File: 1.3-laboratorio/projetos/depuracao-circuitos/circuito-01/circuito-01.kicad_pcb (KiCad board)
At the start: 2 copper layers, 14 parts, among them U1 74LS32, U2 7400, U3 74LS386

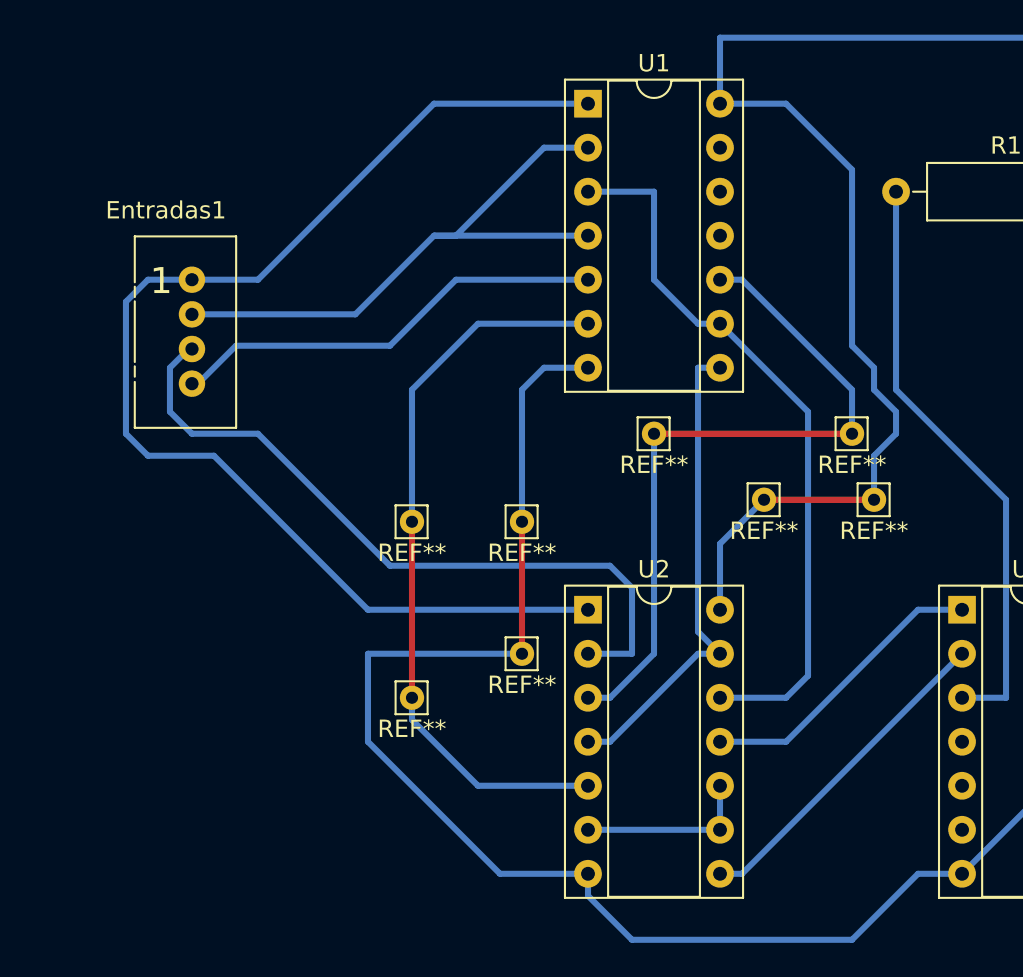
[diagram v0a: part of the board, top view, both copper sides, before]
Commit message: Atualização no esquema/pcb
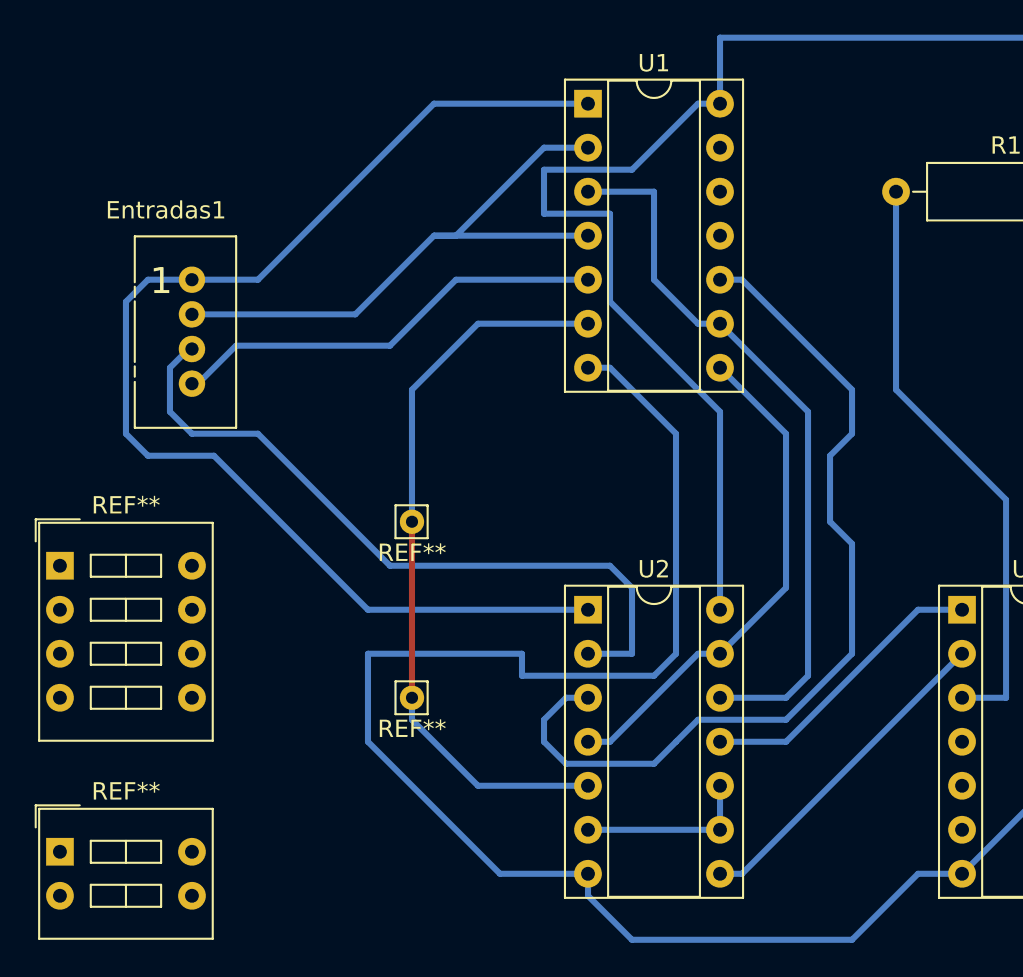
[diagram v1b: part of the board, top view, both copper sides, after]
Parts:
- removed the REF** at (141.0, 133.3)
- removed the REF** at (141.0, 141.0)
- removed the REF** at (148.6, 128.3)
- removed the REF** at (160.0, 128.3)
- removed the REF** at (154.9, 132.1)
- removed the REF** at (161.3, 132.1)
- added REF**: SW_DIP_x4_W7.62mm_Slide, Buttons_Switches_THT:SW_DIP_x4_W7.62mm_Slide, F.Cu at (114.3, 135.9)
- added REF**: SW_DIP_x2_W7.62mm_Slide, Buttons_Switches_THT:SW_DIP_x2_W7.62mm_Slide, F.Cu at (114.3, 152.4)
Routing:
- net (no net): track 35.6 -> 10.2 mm
- net Net-(U1-Pad10): track 30.4 -> 51.8 mm
- net GND: track 99.1 -> 117.2 mm
- net VCC: track 103.3 -> 109.6 mm
- net Net-(U1-Pad8): track 28.0 -> 29.4 mm

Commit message: Alteração PCB/Esquema elétrico
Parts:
- removed Entradas1: Conn_01x04, Connectors:Grove_1x04
- removed REF**: a, Connectors:Pin_d0.7mm_L6.5mm_W1.8mm_FlatFork
- removed REF**: b, Connectors:Pin_d0.7mm_L6.5mm_W1.8mm_FlatFork
- removed REF**: SW_DIP_x4_W7.62mm_Slide, Buttons_Switches_THT:SW_DIP_x4_W7.62mm_Slide
- removed REF**: SW_DIP_x2_W7.62mm_Slide, Buttons_Switches_THT:SW_DIP_x2_W7.62mm_Slide
- added GND: GND, Connectors:Pin_d0.7mm_L6.5mm_W1.8mm_FlatFork, F.Cu at (120.7, 148.6)
- added J1: J1, Connectors:Pin_d0.7mm_L6.5mm_W1.8mm_FlatFork, F.Cu at (127.0, 153.7)
- added J1: J1, Connectors:Pin_d0.7mm_L6.5mm_W1.8mm_FlatFork, F.Cu at (127.0, 158.8)
- added J2: J2, Connectors:Pin_d0.7mm_L6.5mm_W1.8mm_FlatFork, F.Cu at (148.6, 144.8)
- added J2: J2, Connectors:Pin_d0.7mm_L6.5mm_W1.8mm_FlatFork, F.Cu at (148.6, 137.2)
- added R2: R, Resistors_THT:R_Axial_DIN0309_L9.0mm_D3.2mm_P12.70mm_Horizontal, F.Cu at (129.5, 116.8)
- added R3: R, Resistors_THT:R_Axial_DIN0309_L9.0mm_D3.2mm_P12.70mm_Horizontal, F.Cu at (134.6, 116.8)
- added R4: R, Resistors_THT:R_Axial_DIN0309_L9.0mm_D3.2mm_P12.70mm_Horizontal, F.Cu at (142.2, 162.6)
- added R5: R, Resistors_THT:R_Axial_DIN0309_L9.0mm_D3.2mm_P12.70mm_Horizontal, F.Cu at (135.9, 162.6)
- added SW1: SW_DIP_x04, Buttons_Switches_THT:SW_DIP_x4_W7.62mm_Slide, F.Cu at (130.8, 144.8)
- added VCC: VCC 5V, Connectors:Pin_d0.7mm_L6.5mm_W1.8mm_FlatFork, F.Cu at (124.5, 148.6)
- moved R1 28.8 mm to (184.2, 133.3)
- moved D1 22.5 mm to (189.2, 139.7)
- moved U1 12.0 mm to (154.9, 115.6)
- moved U3 10.2 mm to (171.4, 129.5)
- moved U2 10.2 mm to (154.9, 139.7)
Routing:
- net +5V: track 0.00 -> 103.8 mm
- net Net-(R5-Pad2): track 25.3 -> 112.7 mm
- net GND: track 117.2 -> 175.4 mm
- net Net-(R3-Pad2): track 35.7 -> 86.7 mm
- net VCC: track 109.6 -> 71.8 mm
- net Net-(U1-Pad10): track 51.8 -> 23.7 mm
- net Net-(U1-Pad3): track 41.8 -> 66.0 mm
- net Net-(R1-Pad1): track 34.4 -> 13.2 mm
- net Net-(R4-Pad2): track 41.5 -> 52.0 mm
- net (no net): track 10.2 -> 0.00 mm
- net Net-(U2-Pad8): track 19.2 -> 28.8 mm
- net Net-(R4-Pad1): track 0.00 -> 8.89 mm
- net Net-(U1-Pad8): track 29.4 -> 22.2 mm
- net Net-(U2-Pad11): track 17.1 -> 22.2 mm
- net Net-(U2-Pad10): track 10.2 -> 11.2 mm
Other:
- net class Default: trace_width 0.35 -> 0.4

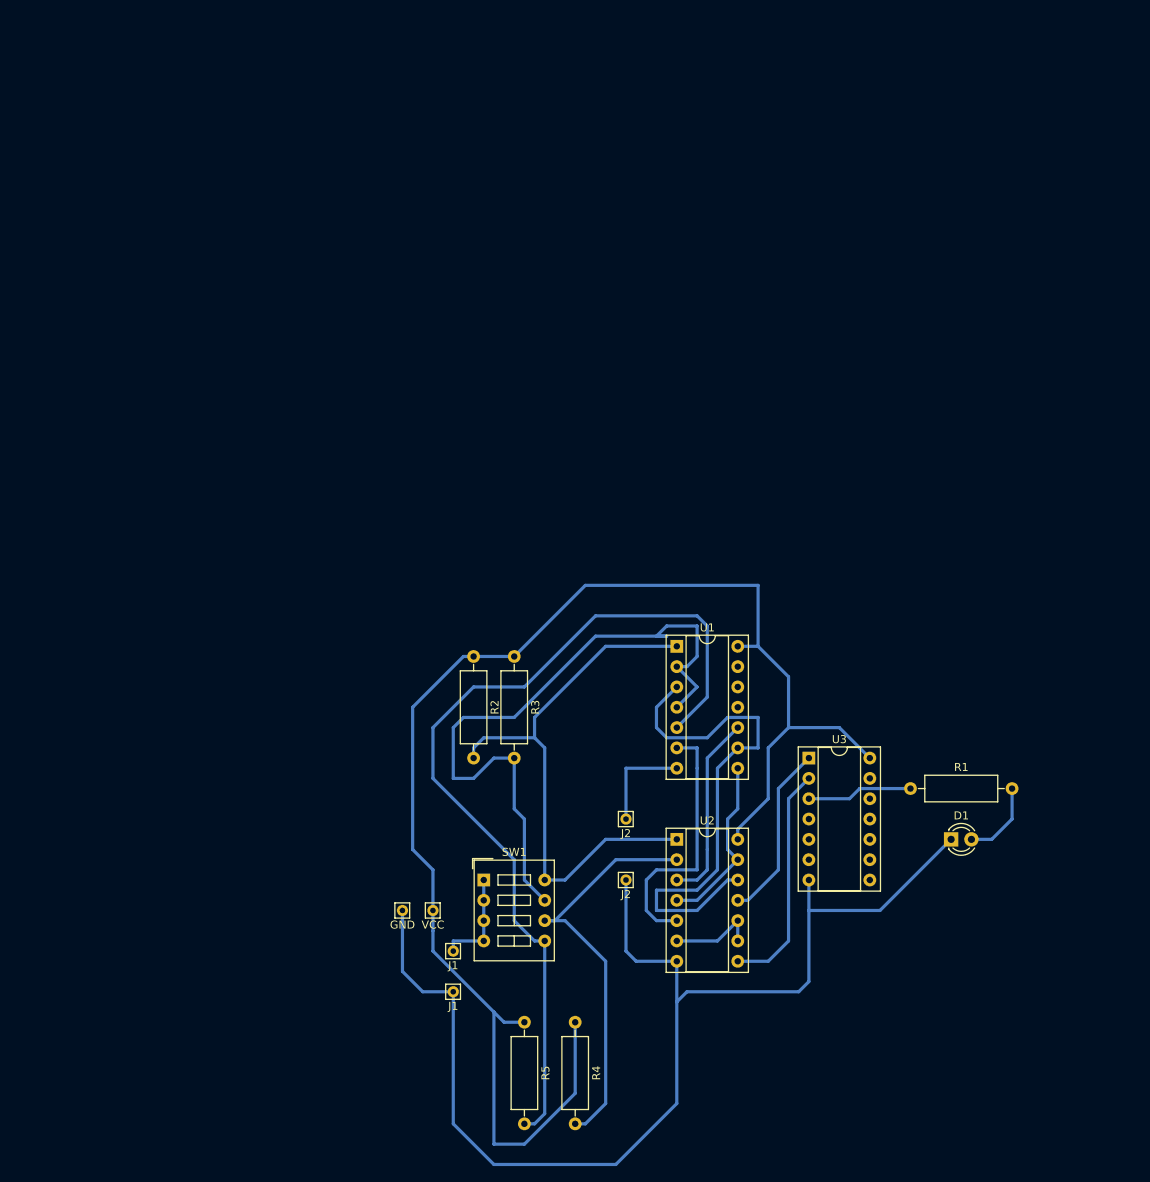
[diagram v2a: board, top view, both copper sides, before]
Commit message: Revisões no esquemático e proposta de novo leiaute da placa.
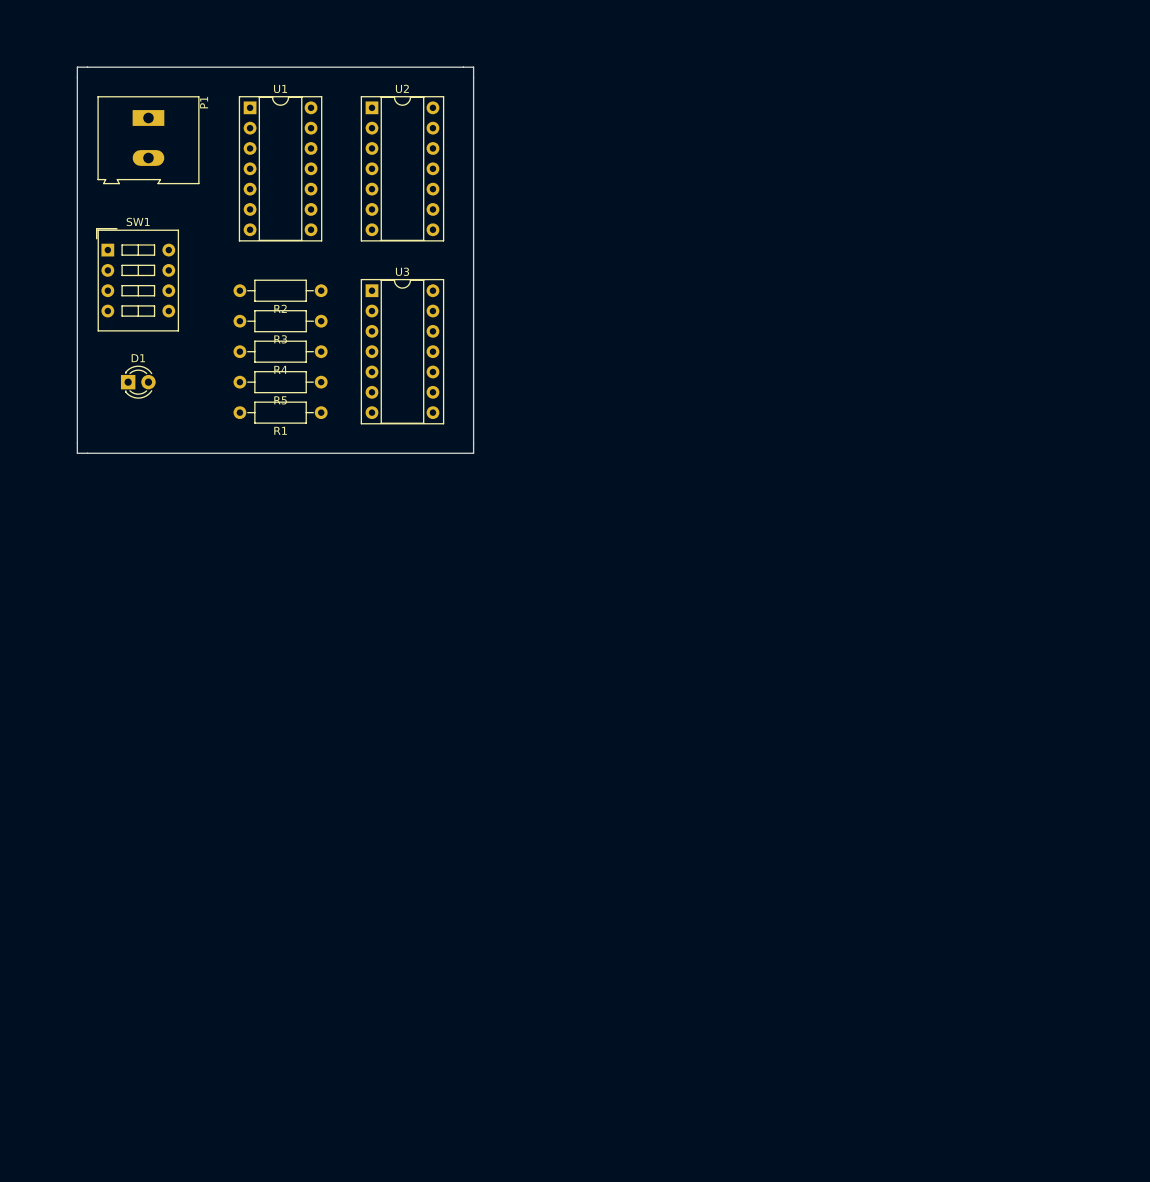
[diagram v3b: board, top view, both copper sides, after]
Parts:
- removed GND: GND, Connectors:Pin_d0.7mm_L6.5mm_W1.8mm_FlatFork
- removed J1 (x2): J1, Connectors:Pin_d0.7mm_L6.5mm_W1.8mm_FlatFork
- removed J2 (x2): J2, Connectors:Pin_d0.7mm_L6.5mm_W1.8mm_FlatFork
- removed VCC: VCC 5V, Connectors:Pin_d0.7mm_L6.5mm_W1.8mm_FlatFork
- added P1: CONN_01X02, Terminal_Blocks:TerminalBlock_Altech_AK300-2_P5.00mm, F.Cu at (88.9, 49.5)
- R1, R2, R3, R4, R5: footprint Resistors_THT:R_Axial_DIN0309_L9.0mm_D3.2mm_P12.70mm_Horizontal -> Resistors_ThroughHole:R_Axial_DIN0207_L6.3mm_D2.5mm_P10.16mm_Horizontal
- SW1: footprint Buttons_Switches_THT:SW_DIP_x4_W7.62mm_Slide -> Buttons_Switches_ThroughHole:SW_DIP_x4_W7.62mm_Slide
- moved D1 117.7 mm to (86.4, 82.5)
- moved U2 99.1 mm to (116.8, 48.3)
- moved SW1 91.7 mm to (83.8, 66.0)
- moved R4 89.6 mm to (110.5, 78.7), turned to 180 degrees
- moved R1 87.4 mm to (110.5, 86.4), turned to 180 degrees
- moved U1 85.9 mm to (101.6, 48.3)
- moved R5 83.9 mm to (110.5, 82.5), turned to 180 degrees
- moved U3 80.0 mm to (116.8, 71.1)
- moved R2 49.5 mm to (110.5, 71.1), turned to 180 degrees
- moved R3 48.4 mm to (110.5, 74.9), turned to 180 degrees
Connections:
- R2 pad 1: +5V -> VCC
- R3 pad 1: +5V -> VCC
- R4 pad 1: Net-(R4-Pad1) -> VCC
- R5 pad 1: +5V -> VCC
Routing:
- net GND: track 175.4 -> 0.00 mm
- net Net-(R5-Pad2): track 112.7 -> 0.00 mm
- net +5V: track 103.8 -> 0.00 mm
- net Net-(R3-Pad2): track 86.7 -> 0.00 mm
- net VCC: track 71.8 -> 0.00 mm
- net Net-(R2-Pad2): track 70.3 -> 0.00 mm
- net Net-(U1-Pad3): track 66.0 -> 0.00 mm
- net Net-(R4-Pad2): track 52.0 -> 0.00 mm
- net Net-(U1-Pad6): track 32.8 -> 0.00 mm
- net Net-(U2-Pad8): track 28.8 -> 0.00 mm
- net Net-(U1-Pad10): track 23.7 -> 0.00 mm
- net Net-(U1-Pad8): track 22.2 -> 0.00 mm
- net Net-(U2-Pad11): track 22.2 -> 0.00 mm
- net Net-(R1-Pad1): track 13.2 -> 0.00 mm
- net Net-(U2-Pad10): track 11.2 -> 0.00 mm
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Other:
- board outline added: 49.5 x 48.3 mm
- net class Alimentacao added: clearance 1, trace_width 1.5, via_dia 0.6, via_drill 0.4
- net class Default: clearance 0.2 -> 0.5; trace_width 0.4 -> 1; via_dia 1 -> 0.6
- rule trace_clearance: 0.2 -> 0.5

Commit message: Atualização PCB
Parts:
- added J1: J1, Connectors:Pin_d0.7mm_L6.5mm_W1.8mm_FlatFork, F.Cu at (81.3, 61.0)
- added J1: J1, Connectors:Pin_d0.7mm_L6.5mm_W1.8mm_FlatFork, F.Cu at (97.8, 61.0)
- added J2: J2, Connectors:Pin_d0.7mm_L6.5mm_W1.8mm_FlatFork, F.Cu at (106.7, 41.9)
- added J2: J2, Connectors:Pin_d0.7mm_L6.5mm_W1.8mm_FlatFork, F.Cu at (114.3, 41.9)
- added J3: J3, Connectors:Pin_d0.7mm_L6.5mm_W1.8mm_FlatFork, F.Cu at (99.1, 43.2)
- added J3: J3, Connectors:Pin_d0.7mm_L6.5mm_W1.8mm_FlatFork, F.Cu at (111.8, 43.2)
- added J4: J4, Connectors:Pin_d0.7mm_L6.5mm_W1.8mm_FlatFork, F.Cu at (125.7, 44.5)
- added J4: J4, Connectors:Pin_d0.7mm_L6.5mm_W1.8mm_FlatFork, F.Cu at (106.7, 44.5)
- moved P1 5.08 mm to (83.8, 49.5)
- moved SW1 5.08 mm to (78.7, 66.0)
- moved U2 2.54 mm to (119.4, 48.3)
- moved U3 2.54 mm to (119.4, 71.1)
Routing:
- net VCC: track 0.00 -> 219.8 mm
- net GND: track 0.00 -> 124.8 mm
- net Net-(R4-Pad2): track 0.00 -> 69.9 mm
- net Net-(R2-Pad2): track 0.00 -> 66.0 mm
- net (no net): track 0.00 -> 55.9 mm
- net Net-(R3-Pad2): track 0.00 -> 55.6 mm
- net Net-(U1-Pad3): track 0.00 -> 42.5 mm
- net Net-(R5-Pad2): track 0.00 -> 41.8 mm
- net Net-(R1-Pad1): track 0.00 -> 26.2 mm
- net Net-(U2-Pad11): track 0.00 -> 25.7 mm
- net Net-(U1-Pad8): track 0.00 -> 25.3 mm
- net Net-(U1-Pad6): track 0.00 -> 24.5 mm
- net Net-(U2-Pad8): track 0.00 -> 20.9 mm
- net Net-(D1-Pad2): track 0.00 -> 14.5 mm
- net Net-(U1-Pad10): track 0.00 -> 12.3 mm
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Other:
- board size 49.5 x 48.3 mm -> 63.5 x 58.4 mm
- net class Alimentacao: clearance 1 -> 0.5; trace_width 1.5 -> 1

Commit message: Ajustes PCB
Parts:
- moved P1 6.48 mm to (82.5, 43.2)
- moved D1 5.08 mm to (81.3, 82.5)
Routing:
- net GND: track 124.8 -> 131.4 mm
- net VCC: track 219.8 -> 224.2 mm
- net Net-(D1-Pad2): track 14.5 -> 18.1 mm
- net Net-(R3-Pad2): track 55.6 -> 57.4 mm
- net Net-(U2-Pad11): track 25.7 -> 24.2 mm
- net Net-(U2-Pad8): track 20.9 -> 20.2 mm
- net Net-(U1-Pad3): track 42.5 -> 41.8 mm
